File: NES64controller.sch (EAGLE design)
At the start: 10 parts, among them CN1 NES64_CONNECTOR

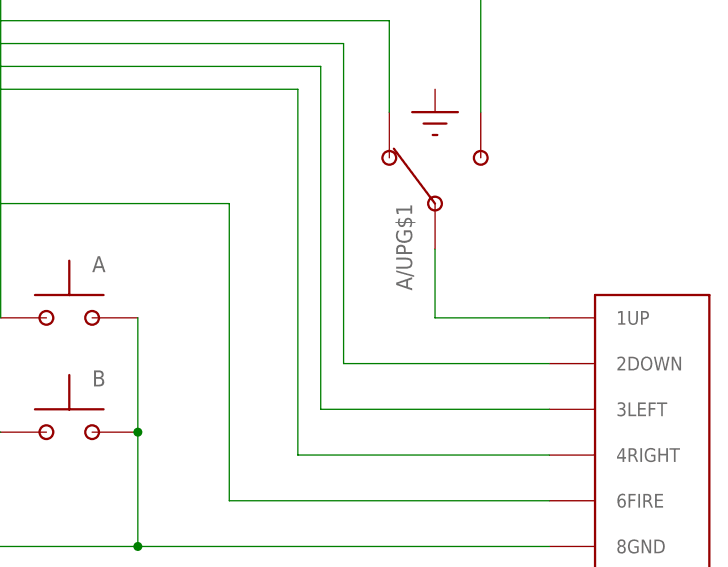
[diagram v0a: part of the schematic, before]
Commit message: Adjustment of hole size in lower right corner and edge notches to fit USB controller case; slight correcting translation of top holes and middle small hole downwards; removing small area of solder mask from middle of button contact areas; adjusting distance between switch pads
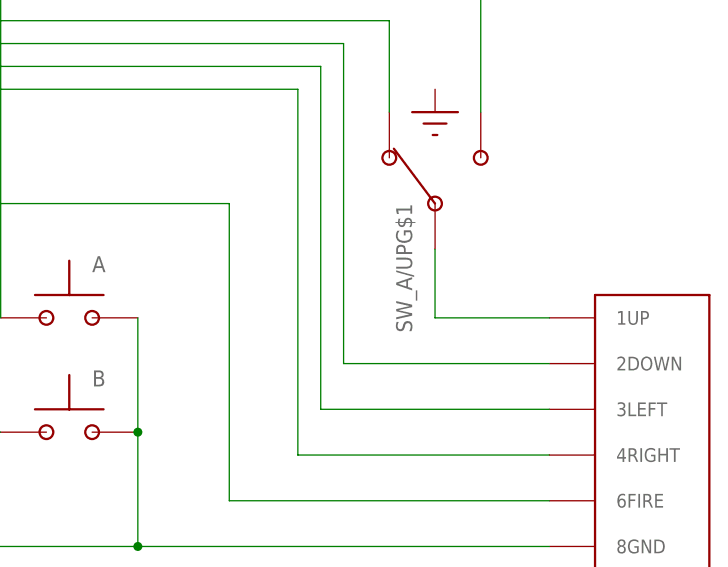
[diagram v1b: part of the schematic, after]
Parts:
- renumbered A/UP to SW_A/UP
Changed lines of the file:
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@@
 <part name="B" library="Thomas" deviceset="RUBBERBUTTON_CONTACTAREA_9MM" device=""/>
 <part name="CN1" library="Thomas" deviceset="NES64_CONNECTOR" device=""/>
-<part name="A/UP" library="Thomas" deviceset="TOGGLESWITCH_SPDT_SMALL_90DEG" device=""/>
+<part name="SW_A/UP" library="Thomas" deviceset="TOGGLESWITCH_SPDT_SMALL_90DEG" device=""/>
 </parts>
 <sheets>
@@
 <attribute name="NAME" x="129.54" y="10.16" size="1.778" layer="95" align="top-center"/>
 </instance>
-<instance part="A/UP" gate="G$2" x="106.68" y="76.2" smashed="yes"/>
-<instance part="A/UP" gate="G$1" x="106.68" y="66.04" smashed="yes" rot="R90">
+<instance part="SW_A/UP" gate="G$2" x="106.68" y="76.2" smashed="yes"/>
+<instance part="SW_A/UP" gate="G$1" x="106.68" y="66.04" smashed="yes" rot="R90">
 <attribute name="NAME" x="104.14" y="63.5" size="1.778" layer="95" rot="R90" align="bottom-right"/>
 </instance>
@@
 <wire x1="-10.16" y1="83.82" x2="-10.16" y2="63.5" width="0.1524" layer="91"/>
 <wire x1="-10.16" y1="63.5" x2="-7.62" y2="63.5" width="0.1524" layer="91"/>
-<pinref part="A/UP" gate="G$1" pin="A"/>
+<pinref part="SW_A/UP" gate="G$1" pin="A"/>
 </segment>
 </net>
@@
 <wire x1="58.42" y1="50.8" x2="58.42" y2="88.9" width="0.1524" layer="91"/>
 <wire x1="58.42" y1="88.9" x2="111.76" y2="88.9" width="0.1524" layer="91"/>
-<pinref part="A/UP" gate="G$1" pin="B"/>
+<pinref part="SW_A/UP" gate="G$1" pin="B"/>
 <wire x1="111.76" y1="88.9" x2="111.76" y2="73.66" width="0.1524" layer="91"/>
 </segment>
@@
 <net name="N$2" class="0">
 <segment>
-<pinref part="A/UP" gate="G$1" pin="N"/>
+<pinref part="SW_A/UP" gate="G$1" pin="N"/>
 <wire x1="106.68" y1="58.42" x2="106.68" y2="50.8" width="0.1524" layer="91"/>
 <pinref part="CN1" gate="G$1" pin="1UP"/>
